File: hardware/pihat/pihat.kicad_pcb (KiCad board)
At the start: 2 copper layers, 85 x 56 mm, 45 parts, among them P1 CONN_13X2, P2 USB_OTG, P3 BATT, U1 MCP73833, U2 TPS61027, U3 SC189, U4 Si4464, X1 30MHz

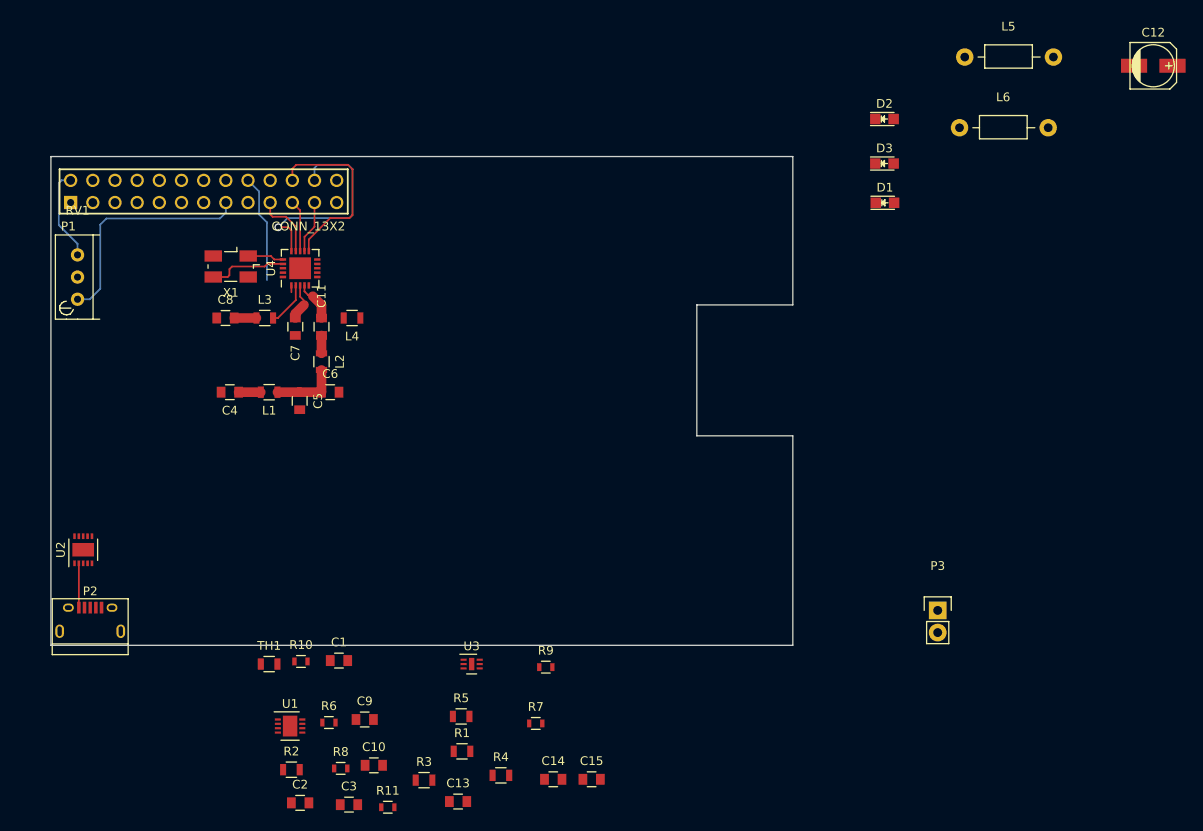
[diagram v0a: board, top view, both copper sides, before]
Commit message: Added a bit more to the routing.
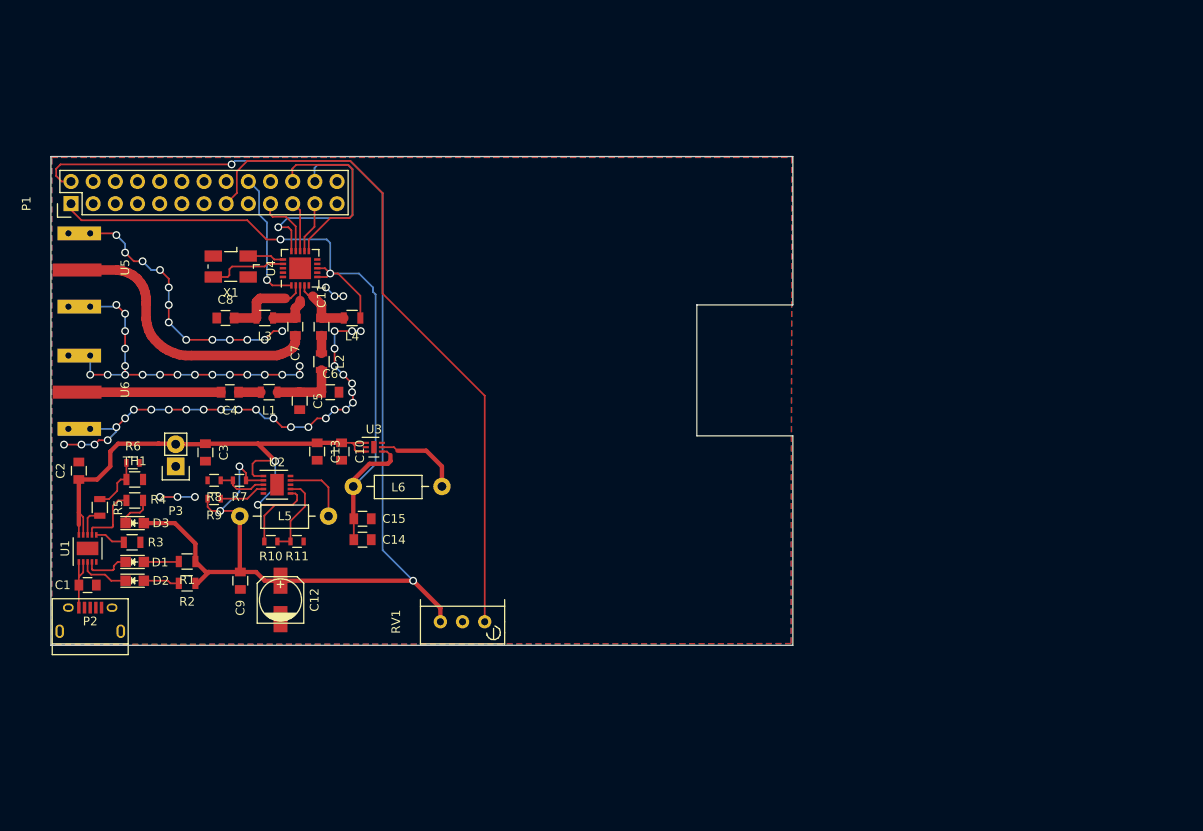
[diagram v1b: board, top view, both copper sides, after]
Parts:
- added U5: SMA_Edge_Mount, RF BW Filter:SMA_Edge_Mount, F.Cu at (146.5, 138.0)
- added U6: SMA_Edge_Mount, RF BW Filter:SMA_Edge_Mount, F.Cu at (146.5, 152.0)
- P1: footprint pin_array_13x2 -> Pin_Headers:Pin_Header_Straight_2x13
- U1: footprint Housings_DFN_QFN:DFN-8-1EP_3x3mm_Pitch0.5mm -> Housings_DFN_QFN:DFN-10-1EP_3x3mm_Pitch0.5mm
- moved C12 117.2 mm to (169.8, 175.8), turned to 90 degrees
- moved D2 100.9 mm to (153.1, 173.6)
- moved L5 98.2 mm to (170.3, 166.2), turned to 180 degrees
- moved D1 95.3 mm to (153.1, 171.4)
- moved D3 95.3 mm to (153.1, 167.0)
- moved P3 88.8 mm to (157.8, 160.5), turned to 180 degrees
- moved L6 80.6 mm to (183.3, 162.8), turned to 180 degrees
- moved RV1 59.5 mm to (193.2, 178.3), turned to 90 degrees
- moved R4 52.5 mm to (153.1, 164.4), turned to 180 degrees
- moved R5 47.8 mm to (149.1, 165.2), turned to 270 degrees
- moved C2 45.7 mm to (146.7, 161.0), turned to 90 degrees
- moved R7 43.9 mm to (165.1, 162.1), turned to 180 degrees
- moved C3 43.6 mm to (161.2, 158.9), turned to 270 degrees
- moved C13 43.2 mm to (174.0, 158.8), turned to 270 degrees
- moved R3 43.1 mm to (152.8, 169.2)
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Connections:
- C4 pad 2: (no net) -> TXO
- C7 pad 2: (no net) -> RXI
- P1 pad 1: (no net) -> +3V3
- P3 pad 2: (no net) -> VBAT
- R5 pad 2: (no net) -> Net-(R5-Pad2)
- U1 pad 7: (no net) -> Net-(R4-Pad2)
- U1 pad 8: Net-(R4-Pad2) -> Net-(R5-Pad2)
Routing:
- net 5VU: track 15.7 -> 159.5 mm, vias 0 -> 4
- net GND: track 0.00 -> 130.3 mm, vias 0 -> 67
- net +3V3: track 0.00 -> 89.3 mm, vias 0 -> 2
- net VBAT: track 0.00 -> 72.0 mm, vias 0 -> 2
- net VOL: track 26.6 -> 76.9 mm
- net RXI: track 0.00 -> 32.7 mm
- net TXO: track 0.00 -> 16.5 mm
- net Net-(L6-Pad1): track 0.00 -> 10.1 mm
- net Net-(R10-Pad2): track 0.00 -> 9.54 mm
- net Net-(L5-Pad1): track 0.00 -> 7.98 mm
- net Net-(R4-Pad2): track 0.00 -> 7.43 mm
- net Net-(R5-Pad1): track 0.00 -> 6.41 mm
- net Net-(D2-Pad1): track 0.00 -> 5.86 mm
- net Net-(R7-Pad2): track 0.00 -> 5.84 mm
- net Net-(D1-Pad1): track 0.00 -> 5.37 mm
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- added copper zone on B.Cu, net GND
- added copper zone on F.Cu, net GND

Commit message: Prepared new Board.
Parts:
- added C16: 10nF, Capacitors_SMD:C_0805, F.Cu at (178.1, 134.3)
- added C17: 10nF, Capacitors_SMD:C_0805, F.Cu at (178.1, 137.1)
- L5, L6: footprint Choke_Axial_ThroughHole:Choke_Horizontal_RM10mm -> inductor:BOURNES_SRN4018
- moved L6 3.73 mm to (186.8, 164.2)
- moved X1 2.15 mm to (162.1, 136.8), turned to 270 degrees
- moved R10 1.31 mm to (168.6, 170.4)
- moved R11 1.31 mm to (171.5, 170.4)
- moved L5 1.19 mm to (169.4, 166.9)
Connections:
- C10 pad 1: VBAT -> 5VU
- C13 pad 1: VBAT -> 5VU
- RV1 pad 1: VOL -> GND
- RV1 pad 2: GND -> VOL
- U3 pad 1: VBAT -> 5VU
- U3 pad 3: VBAT -> 5VU
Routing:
- net GND: track 130.3 -> 220.6 mm, vias 67 -> 184
- net VOL: track 76.9 -> 0.00 mm
- net (no net): track 0.00 -> 27.1 mm, vias 0 -> 17
- net +3V3: track 89.3 -> 110.2 mm, vias 2 -> 3
- net nIRQ: track 21.4 -> 7.84 mm
- net Net-(U4-Pad16): track 4.15 -> 16.5 mm
- net nSEL: track 24.5 -> 12.9 mm
- net VBAT: track 72.0 -> 62.4 mm
- net 5VU: track 159.5 -> 154.5 mm
- net Net-(L5-Pad1): track 7.98 -> 12.7 mm
- net SHDN: track 15.4 -> 10.9 mm
- net SDI: track 7.69 -> 4.39 mm
- net Net-(R10-Pad2): track 9.54 -> 12.5 mm, vias 0 -> 2
- net SCLK: track 6.04 -> 3.26 mm
- net Net-(C4-Pad1): track 5.15 -> 2.60 mm
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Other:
- rule via_min_drill: 0.5 -> 0.31
- rule via_min_size: 0.8 -> 0.5
